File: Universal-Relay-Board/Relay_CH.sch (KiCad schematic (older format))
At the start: 9 parts, among them J1 Conn_01x03_Male, J2 Screw_Terminal_01x03, K1 SRD-XXVDC-SL-C, Q1 2N7002

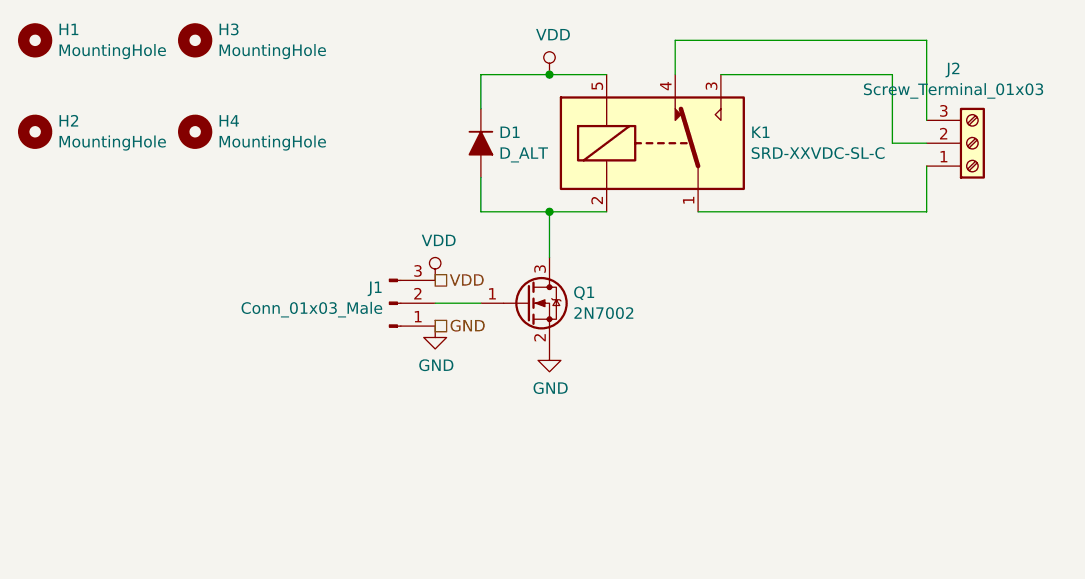
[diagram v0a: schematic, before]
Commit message: single channel done
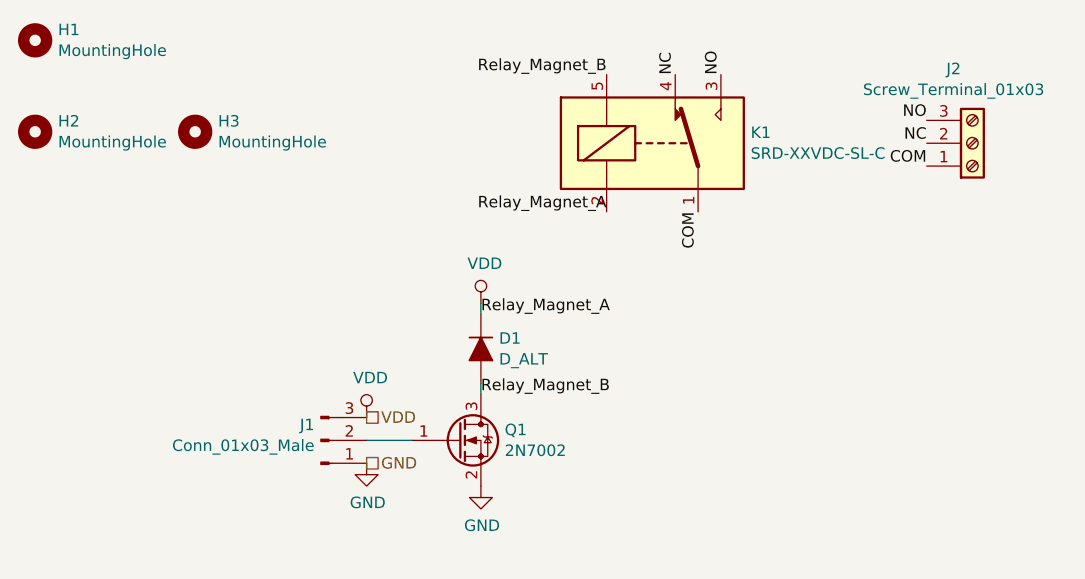
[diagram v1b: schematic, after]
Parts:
- removed H3: MountingHole, MountingHole:MountingHole_2.1mm, symbol Mechanical:MountingHole
- K1: footprint Relay_THT:Relay_StandexMeder_DIP_LowProfile -> Universal-Relay-Board:Relay_SPDT_SANYOU_SRD_Series_Form_C
- renumbered H4 to H3
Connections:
- net VDD: now also K1.2; no longer K1.5
- net COM: now reaches J2.1 (Pin_1), K1.1
- net Relay_Magnet_B: now reaches D1.2 (A), Q1.3 (D)
- net Relay_Magnet_B: now also K1.5; no longer K1.2
- net NC: now reaches J2.2 (Pin_2)
- net NC: now also K1.4; no longer K1.3
- net NO: now reaches J2.3 (Pin_3)
- net NO: now also K1.3; no longer K1.4
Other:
- moved on the sheet: D1, J1, Q1
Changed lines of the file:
@@
 $EndDescr
-$Comp
-L SRD-XXVDC-SL-C:SRD-XXVDC-SL-C K?
-U 1 1 5E8FFE49
-P 5850 3550
-AR Path="/5E8FFE49" Ref="K?"  Part="1"
-AR Path="/5E8FEA39/5E8FFE49" Ref="K1"  Part="1"
-F 0 "K1" H 6280 3596 50  0000 L CNN
-F 1 "SRD-XXVDC-SL-C" H 6280 3505 50  0000 L CNN
-F 2 "Relay_THT:Relay_StandexMeder_DIP_LowProfile" H 6300 3500 50  0001 L CNN
-F 3 "https://standexelectronics.com/wp-content/uploads/datasheet_reed_relay_DIP.pdf" H 5850 3550 50  0001 C CNN
-	1    5850 3550
-	1    0    0    -1
-$EndComp
 $Comp
 L Device:D_ALT D?
 U 1 1 5E8FFE4F
-P 5100 3550
+P 5100 4450
 AR Path="/5E8FFE4F" Ref="D?"  Part="1"
 AR Path="/5E8FEA39/5E8FFE4F" Ref="D1"  Part="1"
-F 0 "D1" V 5054 3629 50  0000 L CNN
-F 1 "D_ALT" V 5145 3629 50  0000 L CNN
-F 2 "Diode_SMD:D_MiniMELF" H 5100 3550 50  0001 C CNN
-F 3 "~" H 5100 3550 50  0001 C CNN
-	1    5100 3550
+F 0 "D1" V 5054 4529 50  0000 L CNN
+F 1 "D_ALT" V 5145 4529 50  0000 L CNN
+F 2 "Diode_SMD:D_MiniMELF" H 5100 4450 50  0001 C CNN
+F 3 "~" H 5100 4450 50  0001 C CNN
+	1    5100 4450
 	0    1    1    0
 $EndComp
@@
 L Transistor_FET:2N7002 Q?
 U 1 1 5E8FFE55
-P 5300 4250
+P 5000 4850
 AR Path="/5E8FFE55" Ref="Q?"  Part="1"
 AR Path="/5E8FEA39/5E8FFE55" Ref="Q1"  Part="1"
-F 0 "Q1" H 5504 4296 50  0000 L CNN
-F 1 "2N7002" H 5504 4205 50  0000 L CNN
-F 2 "Package_TO_SOT_SMD:SOT-23" H 5500 4175 50  0001 L CIN
-F 3 "https://www.fairchildsemi.com/datasheets/2N/2N7002.pdf" H 5300 4250 50  0001 L CNN
-	1    5300 4250
+F 0 "Q1" H 5204 4896 50  0000 L CNN
+F 1 "2N7002" H 5204 4805 50  0000 L CNN
+F 2 "Package_TO_SOT_SMD:SOT-23" H 5200 4775 50  0001 L CIN
+F 3 "https://www.fairchildsemi.com/datasheets/2N/2N7002.pdf" H 5000 4850 50  0001 L CNN
+	1    5000 4850
 	1    0    0    -1
 $EndComp
@@
 L Connector:Conn_01x03_Male J?
 U 1 1 5E8FFE61
-P 4700 4250
+P 4400 4850
 AR Path="/5E8FFE61" Ref="J?"  Part="1"
 AR Path="/5E8FEA39/5E8FFE61" Ref="J1"  Part="1"
-F 0 "J1" H 4672 4182 50  0000 R CNN
-F 1 "Conn_01x03_Male" H 4672 4273 50  0000 R CNN
-F 2 "Connector_PinSocket_2.54mm:PinSocket_1x03_P2.54mm_Vertical" H 4700 4250 50  0001 C CNN
-F 3 "~" H 4700 4250 50  0001 C CNN
-	1    4700 4250
+F 0 "J1" H 4372 4782 50  0000 R CNN
+F 1 "Conn_01x03_Male" H 4372 4873 50  0000 R CNN
+F 2 "Connector_PinSocket_2.54mm:PinSocket_1x03_P2.54mm_Vertical" H 4400 4850 50  0001 C CNN
+F 3 "~" H 4400 4850 50  0001 C CNN
+	1    4400 4850
 	1    0    0    1
 $EndComp
@@
 L power:GND #PWR?
 U 1 1 5E8FFE67
-P 4900 4350
+P 4600 4950
 AR Path="/5E8FFE67" Ref="#PWR?"  Part="1"
 AR Path="/5E8FEA39/5E8FFE67" Ref="#PWR02"  Part="1"
-F 0 "#PWR02" H 4900 4100 50  0001 C CNN
-F 1 "GND" H 4905 4177 50  0000 C CNN
-F 2 "" H 4900 4350 50  0001 C CNN
-F 3 "" H 4900 4350 50  0001 C CNN
-	1    4900 4350
+F 0 "#PWR02" H 4600 4700 50  0001 C CNN
+F 1 "GND" H 4605 4777 50  0000 C CNN
+F 2 "" H 4600 4950 50  0001 C CNN
+F 3 "" H 4600 4950 50  0001 C CNN
+	1    4600 4950
 	1    0    0    -1
 $EndComp
@@
 L power:VDD #PWR?
 U 1 1 5E8FFE6D
-P 4900 4150
+P 4600 4750
 AR Path="/5E8FFE6D" Ref="#PWR?"  Part="1"
 AR Path="/5E8FEA39/5E8FFE6D" Ref="#PWR01"  Part="1"
-F 0 "#PWR01" H 4900 4000 50  0001 C CNN
-F 1 "VDD" H 4917 4323 50  0000 C CNN
-F 2 "" H 4900 4150 50  0001 C CNN
-F 3 "" H 4900 4150 50  0001 C CNN
-	1    4900 4150
+F 0 "#PWR01" H 4600 4600 50  0001 C CNN
+F 1 "VDD" H 4617 4923 50  0000 C CNN
+F 2 "" H 4600 4750 50  0001 C CNN
+F 3 "" H 4600 4750 50  0001 C CNN
+	1    4600 4750
 	1    0    0    -1
 $EndComp
-Wire Wire Line
-	5100 3400 5100 3250
-Wire Wire Line
-	5100 3250 5400 3250
-Wire Wire Line
-	5100 3700 5100 3850
-Wire Wire Line
-	5100 3850 5400 3850
-Wire Wire Line
-	6050 3850 7050 3850
-Wire Wire Line
-	7050 3850 7050 3650
-Wire Wire Line
-	5950 3250 5950 3100
-Wire Wire Line
-	5950 3100 7050 3100
-Wire Wire Line
-	7050 3100 7050 3450
-Wire Wire Line
-	6150 3250 6900 3250
-Wire Wire Line
-	6900 3250 6900 3550
-Wire Wire Line
-	6900 3550 7050 3550
-Wire Wire Line
-	5400 4050 5400 3850
-Connection ~ 5400 3850
-Wire Wire Line
-	5400 3850 5650 3850
 $Comp
 L power:GND #PWR?
 U 1 1 5E8FFE82
-P 5400 4450
+P 5100 5050
 AR Path="/5E8FFE82" Ref="#PWR?"  Part="1"
 AR Path="/5E8FEA39/5E8FFE82" Ref="#PWR04"  Part="1"
-F 0 "#PWR04" H 5400 4200 50  0001 C CNN
-F 1 "GND" H 5405 4277 50  0000 C CNN
-F 2 "" H 5400 4450 50  0001 C CNN
-F 3 "" H 5400 4450 50  0001 C CNN
-	1    5400 4450
+F 0 "#PWR04" H 5100 4800 50  0001 C CNN
+F 1 "GND" H 5105 4877 50  0000 C CNN
+F 2 "" H 5100 5050 50  0001 C CNN
+F 3 "" H 5100 5050 50  0001 C CNN
+	1    5100 5050
 	1    0    0    -1
 $EndComp
@@
 L power:VDD #PWR?
 U 1 1 5E8FFE88
-P 5400 3250
+P 5100 4250
 AR Path="/5E8FFE88" Ref="#PWR?"  Part="1"
 AR Path="/5E8FEA39/5E8FFE88" Ref="#PWR03"  Part="1"
-F 0 "#PWR03" H 5400 3100 50  0001 C CNN
-F 1 "VDD" H 5417 3423 50  0000 C CNN
-F 2 "" H 5400 3250 50  0001 C CNN
-F 3 "" H 5400 3250 50  0001 C CNN
-	1    5400 3250
+F 0 "#PWR03" H 5100 4100 50  0001 C CNN
+F 1 "VDD" H 5117 4423 50  0000 C CNN
+F 2 "" H 5100 4250 50  0001 C CNN
+F 3 "" H 5100 4250 50  0001 C CNN
+	1    5100 4250
 	1    0    0    -1
 $EndComp
-Connection ~ 5400 3250
 Wire Wire Line
-	5400 3250 5650 3250
-Wire Wire Line
-	4900 4250 5100 4250
+	4600 4850 4800 4850
 $Comp
 L Mechanical:MountingHole H?
@@
 F 3 "~" H 3150 3100 50  0001 C CNN
 	1    3150 3100
-	1    0    0    -1
-$EndComp
-$Comp
-L Mechanical:MountingHole H?
-U 1 1 5E8FFE97
-P 3850 3100
-AR Path="/5E8FFE97" Ref="H?"  Part="1"
-AR Path="/5E8FEA39/5E8FFE97" Ref="H3"  Part="1"
-F 0 "H3" H 3950 3146 50  0000 L CNN
-F 1 "MountingHole" H 3950 3055 50  0000 L CNN
-F 2 "MountingHole:MountingHole_2.1mm" H 3850 3100 50  0001 C CNN
-F 3 "~" H 3850 3100 50  0001 C CNN
-	1    3850 3100
 	1    0    0    -1
 $EndComp
@@
 P 3850 3500
 AR Path="/5E8FFEA3" Ref="H?"  Part="1"
-AR Path="/5E8FEA39/5E8FFEA3" Ref="H4"  Part="1"
-F 0 "H4" H 3950 3546 50  0000 L CNN
+AR Path="/5E8FEA39/5E8FFEA3" Ref="H3"  Part="1"
+F 0 "H3" H 3950 3546 50  0000 L CNN
 F 1 "MountingHole" H 3950 3455 50  0000 L CNN
 F 2 "MountingHole:MountingHole_2.1mm" H 3850 3500 50  0001 C CNN
@@
 	1    0    0    -1
 $EndComp
-Text HLabel 4900 4150 2    50   UnSpc ~ 0
+Text HLabel 4600 4750 2    50   UnSpc ~ 0
 VDD
-Text HLabel 4900 4350 2    50   UnSpc ~ 0
+Text HLabel 4600 4950 2    50   UnSpc ~ 0
 GND
+$Comp
+L SRD-XXVDC-SL-C:SRD-XXVDC-SL-C K?
+U 1 1 5E8FFE49
+P 5850 3550
+AR Path="/5E8FFE49" Ref="K?"  Part="1"
+AR Path="/5E8FEA39/5E8FFE49" Ref="K1"  Part="1"
+F 0 "K1" H 6280 3596 50  0000 L CNN
+F 1 "SRD-XXVDC-SL-C" H 6280 3505 50  0000 L CNN
+F 2 "Universal-Relay-Board:Relay_SPDT_SANYOU_SRD_Series_Form_C" H 6300 3500 50  0001 L CNN
+F 3 "https://standexelectronics.com/wp-content/uploads/datasheet_reed_relay_DIP.pdf" H 5850 3550 50  0001 C CNN
+	1    5850 3550
+	1    0    0    -1
+$EndComp
+Text Label 5100 4300 0    50   ~ 0
+Relay_Magnet_A
+Wire Wire Line
+	5100 4300 5100 4250
+Wire Wire Line
+	5100 4600 5100 4650
+Text Label 5650 3850 2    50   ~ 0
+Relay_Magnet_A
+Text Label 5650 3250 2    50   ~ 0
+Relay_Magnet_B
+Text Label 5100 4650 0    50   ~ 0
+Relay_Magnet_B
+Text Label 7050 3650 2    50   ~ 0
+COM
+Text Label 7050 3450 2    50   ~ 0
+NO
+Text Label 7050 3550 2    50   ~ 0
+NC
+Text Label 6050 3850 3    50   ~ 0
+COM
+Text Label 6150 3250 1    50   ~ 0
+NO
+Text Label 5950 3250 1    50   ~ 0
+NC
 $EndSCHEMATC

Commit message: multi channel done
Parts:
- added R1: 10K, Resistor_SMD:R_0805_2012Metric, symbol Device:R
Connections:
- net GND: now also R1.2
- net at J1.2 (Pin_2), Q1.1 (G): now also R1.1
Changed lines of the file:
@@
 Text Label 5950 3250 1    50   ~ 0
 NC
+$Comp
+L Device:R R1
+U 1 1 5E94835D
+P 4800 5000
+F 0 "R1" H 4870 5046 50  0000 L CNN
+F 1 "10K" H 4870 4955 50  0000 L CNN
+F 2 "Resistor_SMD:R_0805_2012Metric" V 4730 5000 50  0001 C CNN
+F 3 "~" H 4800 5000 50  0001 C CNN
+	1    4800 5000
+	1    0    0    -1
+$EndComp
+Connection ~ 4800 4850
+$Comp
+L power:GND #PWR?
+U 1 1 5E948910
+P 4800 5150
+AR Path="/5E948910" Ref="#PWR?"  Part="1"
+AR Path="/5E8FEA39/5E948910" Ref="#PWR0101"  Part="1"
+F 0 "#PWR0101" H 4800 4900 50  0001 C CNN
+F 1 "GND" H 4805 4977 50  0000 C CNN
+F 2 "" H 4800 5150 50  0001 C CNN
+F 3 "" H 4800 5150 50  0001 C CNN
+	1    4800 5150
+	1    0    0    -1
+$EndComp
 $EndSCHEMATC
